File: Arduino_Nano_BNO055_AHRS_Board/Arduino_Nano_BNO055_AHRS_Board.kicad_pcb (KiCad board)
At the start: 2 copper layers, 49 x 70 mm, 7 parts, among them J1 Conn_01x04, J3 Conn_01x07_Pin, J4 Conn_01x02_Pin, J5 Conn_01x02_Pin, J6 Conn_01x06_Pin

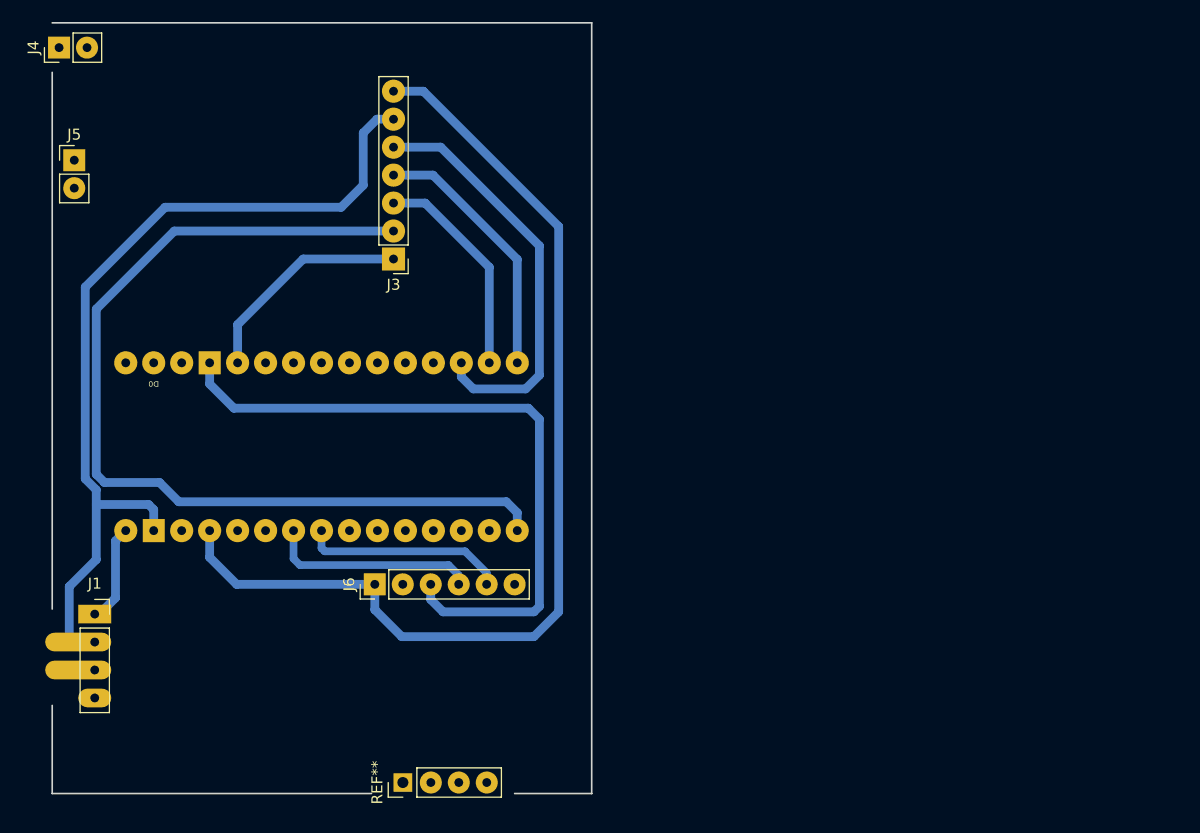
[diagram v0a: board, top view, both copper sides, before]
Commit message: Updates Arduino_Nano_BNO055_AHRS_Board files. The older version required a via to cross two traces. This new version uses a larger PCB blank (one-sided) and no longer requires any vias. I also moved the BNO055 sensor away from the buck power converter (and all the other electronics on the board) to help minimize EMI, which can make it hard for the Magnetometer to calibrate.
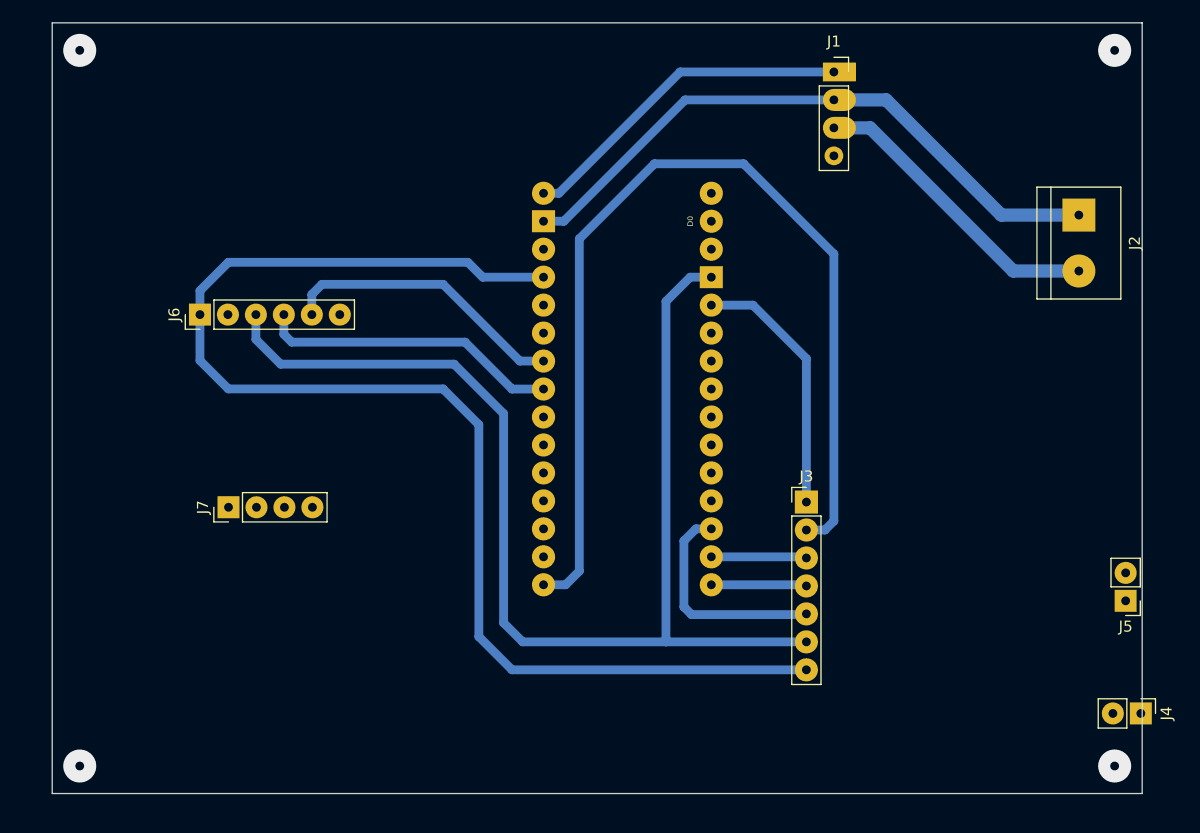
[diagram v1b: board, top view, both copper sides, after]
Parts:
- removed REF**: PinHeader_1x04_P2.54mm_Vertical, Connector_PinHeader_2.54mm:PinHeader_1x04_P2.54mm_Vertical
- added J2: Screw_Terminal_01x02, TerminalBlock:TerminalBlock_bornier-2_P5.08mm, F.Cu at (191.8, 60.2)
- added J7: Conn_01x04_Pin, Connector_PinHeader_2.54mm:PinHeader_1x04_P2.54mm_Vertical, F.Cu at (114.5, 86.8)
- moved J4 115.4 mm to (197.4, 105.5), turned to -90 degrees
- moved J5 103.5 mm to (196.0, 95.2), turned to 180 degrees
- moved J1 83.3 mm to (169.5, 47.2)
- moved J3 43.5 mm to (167.0, 86.3), turned to 0 degrees
- moved J6 29.2 mm to (111.9, 69.2)
- moved XA1 17.5 mm to (150.7, 97.6), turned to 180 degrees
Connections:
- J3 pad 6: GND -> Net-(J3-Pin_6)
- J6 pad 3: Net-(J6-Pin_3) -> Net-(J3-Pin_6)
- XA1 pad A4: Net-(J6-Pin_5) -> Net-(J6-Pin_4)
- XA1 pad A5: Net-(J6-Pin_4) -> Net-(J6-Pin_5)
- XA1 pad GND1: Net-(J6-Pin_3) -> Net-(J3-Pin_6)
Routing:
- net Net-(J3-Pin_6): track 0.00 -> 110.7 mm
- net Net-(J6-Pin_3): track 62.1 -> 0.00 mm
- net +12V: track 1.08 -> 27.6 mm
- net GND: track 80.4 -> 57.5 mm
- net Net-(J3-Pin_7): track 94.5 -> 117.4 mm
- net Net-(J1-Pin_1): track 8.99 -> 30.9 mm
- net Net-(J3-Pin_5): track 38.5 -> 20.4 mm
- net Net-(J3-Pin_4): track 23.8 -> 8.68 mm
- net Net-(J3-Pin_3): track 19.8 -> 9.34 mm
- net Net-(J6-Pin_4): track 19.0 -> 27.4 mm
- net Net-(J6-Pin_5): track 18.6 -> 26.1 mm
- net Net-(J3-Pin_2): track 86.3 -> 90.4 mm
- net Net-(J3-Pin_1): track 20.1 -> 23.7 mm
- net (no net): vias 0 -> 4
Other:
- board size 49 x 70 mm -> 99 x 70 mm
- board text added: "VIN"
- board text removed: "VCC"

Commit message: Split the AOA LED project into two projects - one for the LEDs and one for the Nano board and the MCP2515 CAN board.
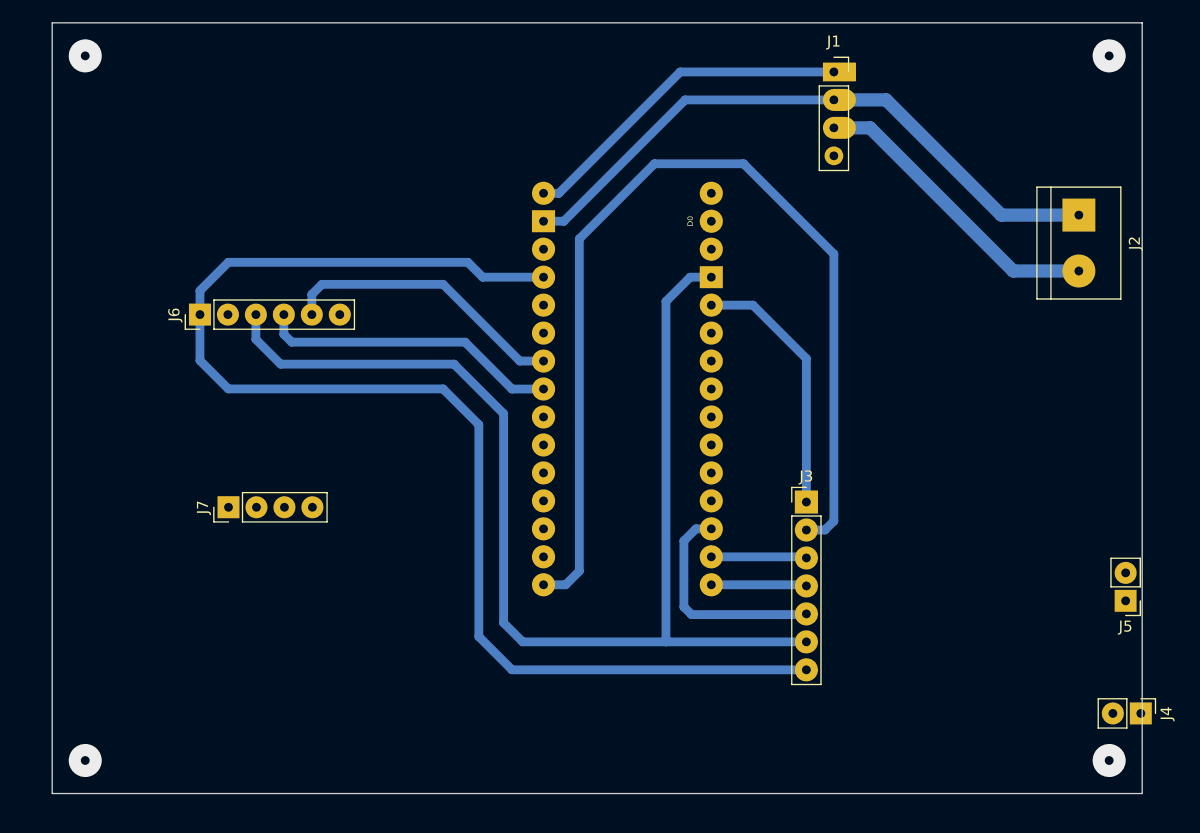
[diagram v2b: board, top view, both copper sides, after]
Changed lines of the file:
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@@
     (style (thickness 0.15) (arrow_length 1.27) (text_position_mode 2) (extension_height 0.58642) (extension_offset 0.5) keep_text_aligned)
   )
-  (via (at 195 45.25) (size 3) (drill 0.8) (layers "F.Cu" "B.Cu") (net 0))
-  (via (at 101 110.25) (size 3) (drill 0.8) (layers "F.Cu" "B.Cu") (net 0))
-  (via (at 101 45.25) (size 3) (drill 0.8) (layers "F.Cu" "B.Cu") (net 0))
-  (via (at 195 110.25) (size 3) (drill 0.8) (layers "F.Cu" "B.Cu") (net 0))
+  (via (at 194.5 45.75) (size 3) (drill 0.8) (layers "F.Cu" "B.Cu") (net 0))
+  (via (at 101.5 109.75) (size 3) (drill 0.8) (layers "F.Cu" "B.Cu") (net 0))
+  (via (at 101.5 45.75) (size 3) (drill 0.8) (layers "F.Cu" "B.Cu") (net 0))
+  (via (at 194.5 109.75) (size 3) (drill 0.8) (layers "F.Cu" "B.Cu") (net 0))
   (segment (start 111.92 73.42) (end 111.92 69.25) (width 0.8) (layer "B.Cu") (net 1))
   (segment (start 140.265 101.515) (end 137.25 98.5) (width 0.8) (layer "B.Cu") (net 1))

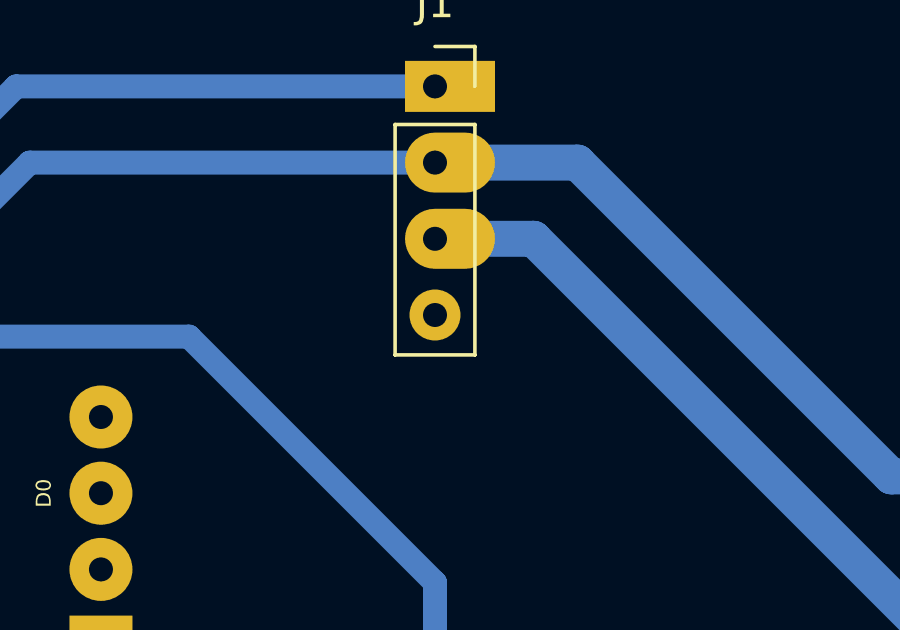
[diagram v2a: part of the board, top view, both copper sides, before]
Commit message: Created a new board for the Wit-Motion WT901B IMU chip.
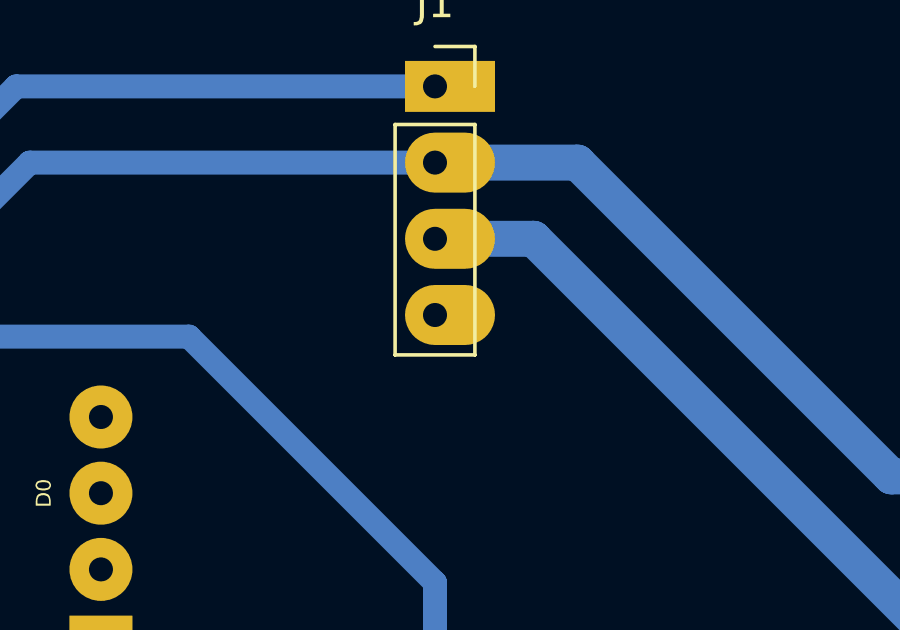
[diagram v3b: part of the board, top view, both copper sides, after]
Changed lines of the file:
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@@
     (pad "3" thru_hole oval (at 0 5.08) (size 3 2) (drill 0.8 (offset 0.5 0)) (layers "*.Cu" "*.Mask")
       (net 28 "+12V") (pinfunction "Pin_3") (pintype "passive"))
-    (pad "4" thru_hole oval (at 0 7.62) (size 1.7 1.7) (drill 0.8) (layers "*.Cu" "*.Mask")
+    (pad "4" thru_hole oval (at 0 7.62) (size 3 2) (drill 0.8 (offset 0.5 0)) (layers "*.Cu" "*.Mask")
       (net 29 "unconnected-(J1-Pin_4-Pad4)") (pinfunction "Pin_4") (pintype "passive"))
     (model "${KICAD6_3DMODEL_DIR}/Connector_PinSocket_2.54mm.3dshapes/PinSocket_1x04_P2.54mm_Vertical.wrl"
@@
   (gr_line (start 187.848318 45.54) (end 187.848318 56.5)
     (stroke (width 0.15) (type default)) (layer "Dwgs.User"))
+  (gr_line (start 197.5 107.5) (end 197.5 112.75)
+    (stroke (width 0.15) (type default)) (layer "Dwgs.User"))
   (gr_line (start 152.615 96.800818) (end 147.74 96.800818)
     (stroke (width 0.15) (type solid)) (layer "Dwgs.User"))
@@
   (gr_line (start 160.245 84.300818) (end 160.245 70.257068)
     (stroke (width 0.15) (type solid)) (layer "Dwgs.User"))
+  (gr_line (start 197.5 97.25) (end 197.5 103.25)
+    (stroke (width 0.15) (type default)) (layer "Dwgs.User"))
+  (gr_line (start 98.5 42.75) (end 197.5 42.75)
+    (stroke (width 0.15) (type default)) (layer "Dwgs.User"))
   (gr_line (start 141.245 67.800818) (end 141.245 71.800818)
     (stroke (width 0.15) (type default)) (layer "Dwgs.User"))
   (gr_line (start 168.075 56.29) (end 168.075 56.51)
     (stroke (width 0.15) (type default)) (layer "Dwgs.User"))
-  (gr_line (start 168.75 107.345) (end 197.6275 107.345)
+  (gr_line (start 164.75 107.345) (end 193 107.345)
     (stroke (width 0.15) (type default)) (layer "Dwgs.User"))
   (gr_line (start 168.075 45.54) (end 187.848318 45.54)
     (stroke (width 0.15) (type default)) (layer "Dwgs.User"))
-  (gr_line (start 171.5 80.345) (end 197.6275 80.345)
+  (gr_line (start 171.5 80.345) (end 196.25 80.345)
     (stroke (width 0.15) (type default)) (layer "Dwgs.User"))
   (gr_line (start 141.245 77.800818) (end 141.245 92.800818)
     (stroke (width 0.15) (type default)) (layer "Dwgs.User"))
   (gr_line (start 168.075 56.51) (end 172.75 56.51)
+    (stroke (width 0.15) (type default)) (layer "Dwgs.User"))
+  (gr_line (start 164.75 107.345) (end 164.75 104.25)
     (stroke (width 0.15) (type default)) (layer "Dwgs.User"))
   (gr_line (start 147.74 96.800818) (end 147.74 94.550818)
     (stroke (width 0.15) (type solid)) (layer "Dwgs.User"))
+  (gr_line (start 98.5 112.75) (end 98.5 42.75)
+    (stroke (width 0.15) (type default)) (layer "Dwgs.User"))
+  (gr_line (start 197.5 112.75) (end 98.5 112.75)
+    (stroke (width 0.15) (type default)) (layer "Dwgs.User"))
+  (gr_line (start 197.5 42.75) (end 197.5 90.25)
+    (stroke (width 0.15) (type default)) (layer "Dwgs.User"))
   (gr_line (start 168.075 45.54) (end 168.075 45.79)
     (stroke (width 0.15) (type default)) (layer "Dwgs.User"))
